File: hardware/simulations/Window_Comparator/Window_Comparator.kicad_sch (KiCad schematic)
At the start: 11 parts, among them U101 Opamp_Dual

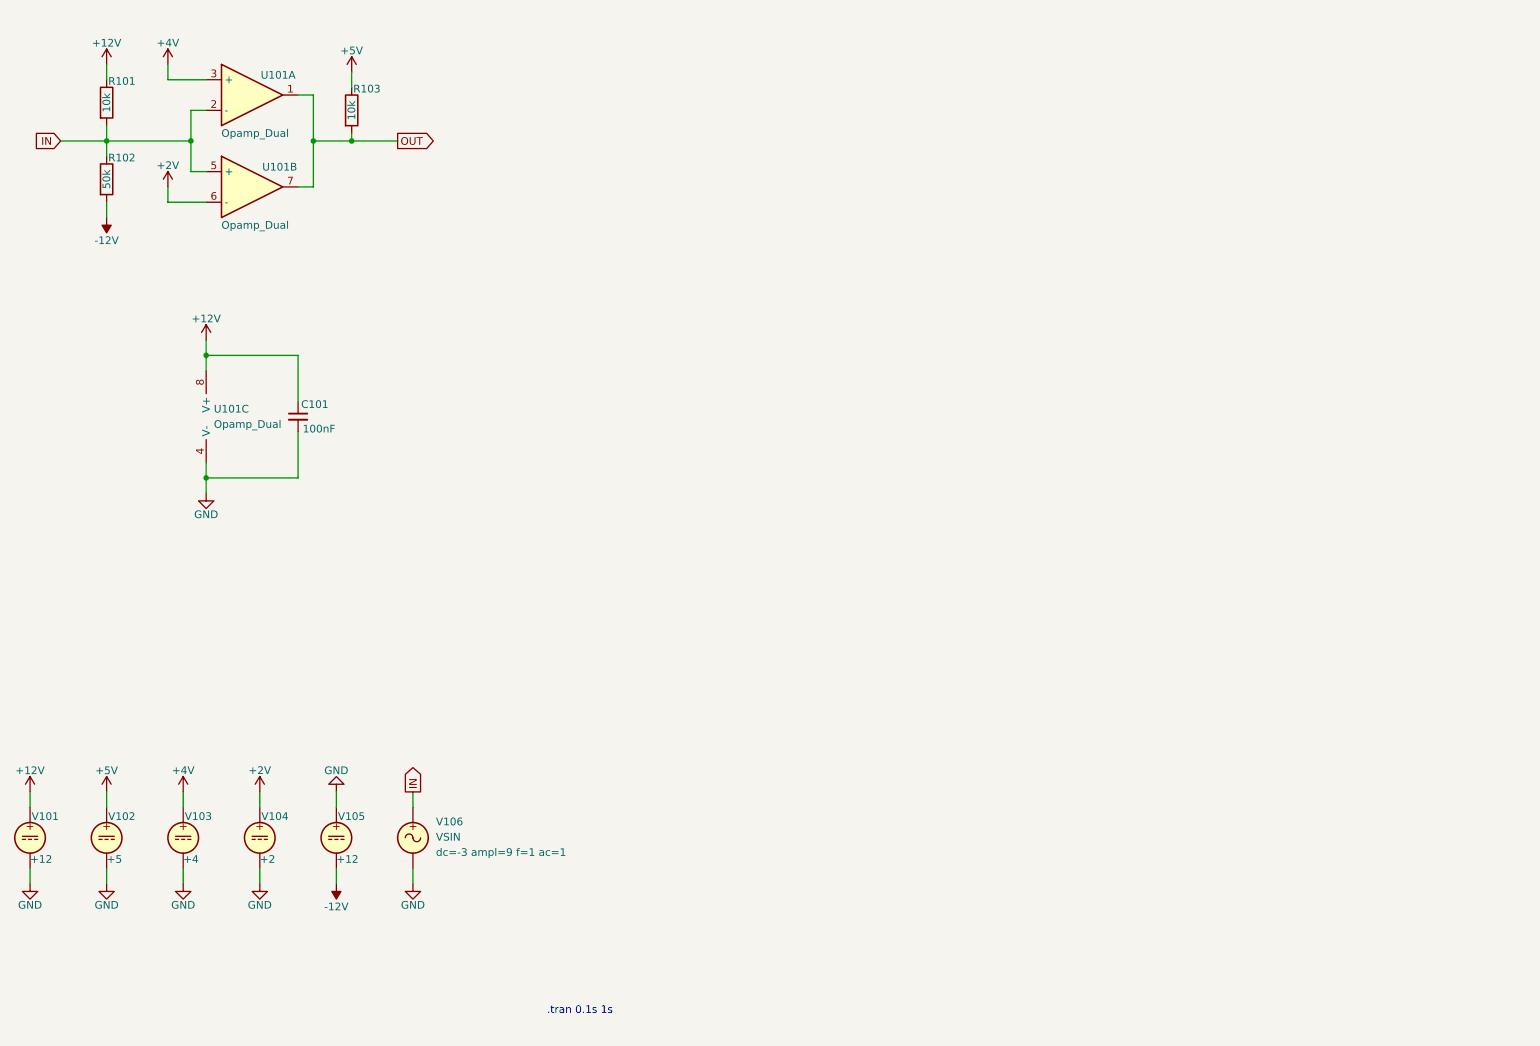
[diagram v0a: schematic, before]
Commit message: Quality assessment - Changes
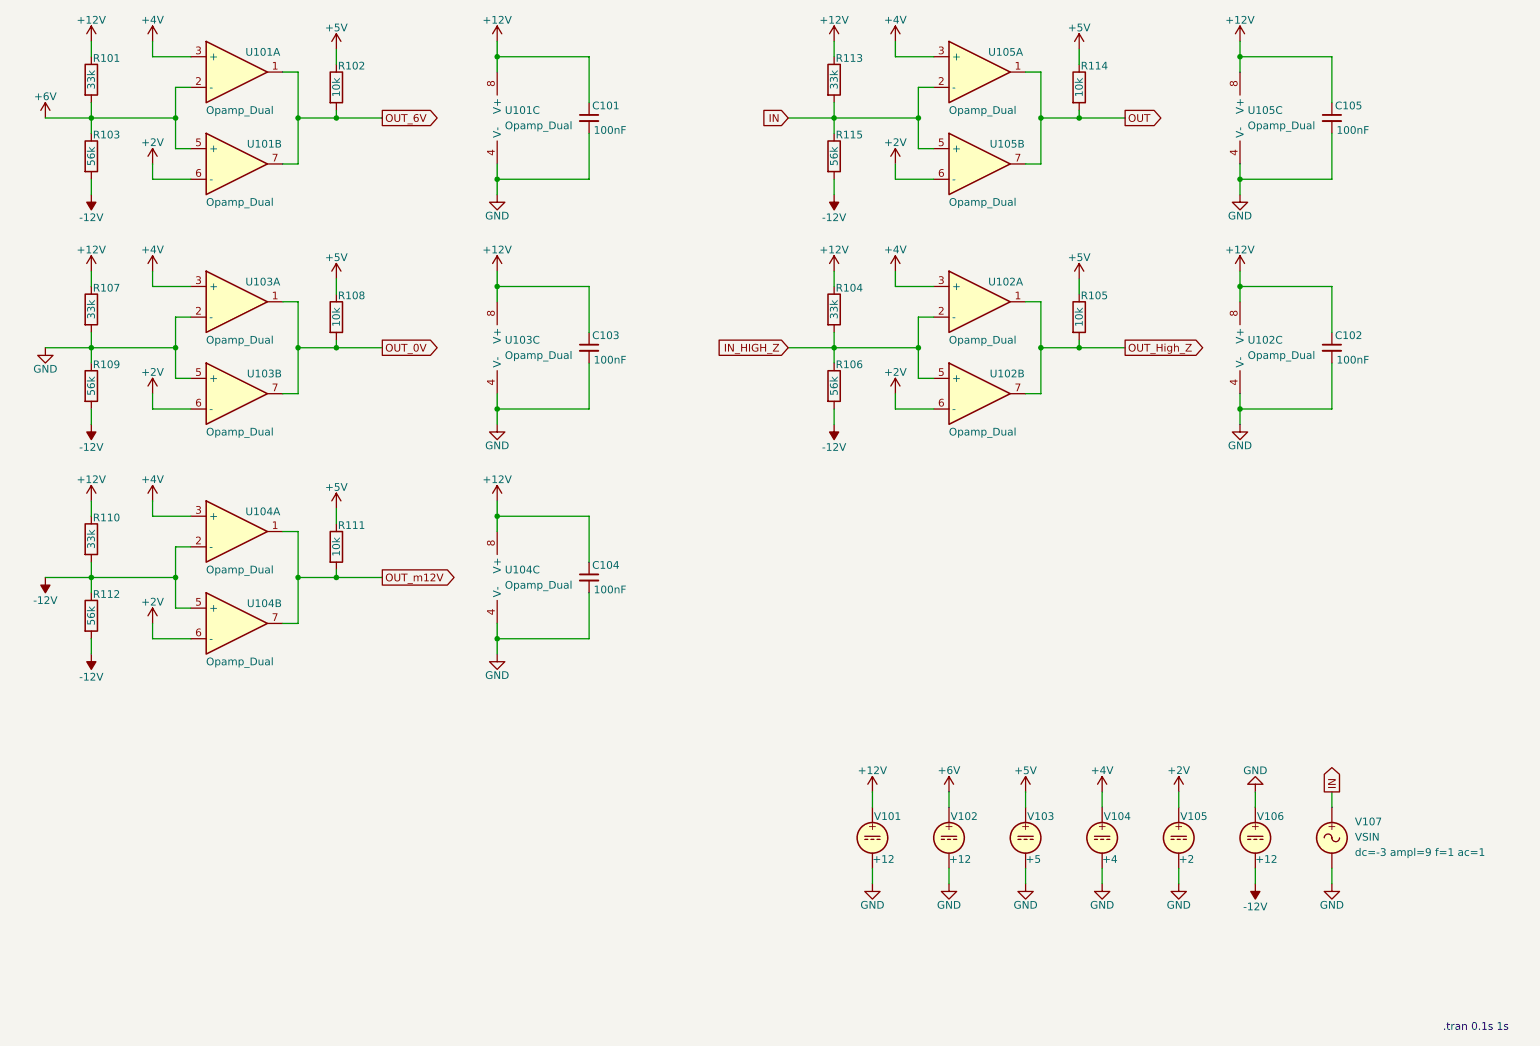
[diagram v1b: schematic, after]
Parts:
- added C102, C103, C104, C105: 100nF, Capacitor_THT:C_Disc_D5.0mm_W2.5mm_P5.00mm, symbol Device:C_Small
- added R104, R107, R110, R113: 33k, Resistor_THT:R_Axial_DIN0207_L6.3mm_D2.5mm_P7.62mm_Horizontal, symbol Device:R
- added R105, R108, R111, R114: 10k, Resistor_THT:R_Axial_DIN0207_L6.3mm_D2.5mm_P7.62mm_Horizontal, symbol Device:R
- added R106, R109, R112, R115: 56k, Resistor_THT:R_Axial_DIN0207_L6.3mm_D2.5mm_P7.62mm_Horizontal, symbol Device:R
- added U102, U103, U104, U105: Opamp_Dual, symbol Device:Opamp_Dual
- added V101: +12, symbol Simulation_SPICE:VDC
- R101: value 10k -> 33k
- R103: renamed from R102; value 50k -> 56k
- renumbered R103 to R102, V101 to V102, V102 to V103, V103 to V104, V104 to V105, V105 to V106, V106 to V107
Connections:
- net +12V: now also C102.1, C103.1, C104.1, C105.1, R104.1, R107.1, R110.1, R113.1, U102.8 (V+), U103.8 (V+), U104.8 (V+), U105.8 (V+), V101.1; no longer V102.1
- net +2V: now also U102.6 (-), U103.6 (-), U104.6 (-), U105.6 (-)
- net +4V: now also U102.3 (+), U103.3 (+), U104.3 (+), U105.3 (+)
- net +5V: now also R105.1, R108.1, R111.1, R114.1
- net -12V: now also R106.2, R109.2, R110.2, R112.1, R112.2, R115.2, U104.2 (-), U104.5 (+)
- net GND: now also C102.2, C103.2, C104.2, C105.2, R107.2, R109.1, U102.4 (V-), U103.2 (-), U103.4 (V-), U103.5 (+), U104.4 (V-), U105.4 (V-), V101.2
- net IN: now also R113.2, R115.1, U105.2 (-), U105.5 (+); no longer R101.2, R103.1, U101.2 (-), U101.5 (+)
- net OUT: now also R114.2, U105.1, U105.7; no longer R102.2, U101.1, U101.7
- new net +6V: R101.2, R103.1, U101.2 (-), U101.5 (+), V102.1
- new net IN_HIGH_Z: R104.2, R106.1, U102.2 (-), U102.5 (+)
- new net OUT_0V: R108.2, U103.1, U103.7
- new net OUT_6V: R102.2, U101.1, U101.7
- new net OUT_High_Z: R105.2, U102.1, U102.7
- new net OUT_m12V: R111.2, U104.1, U104.7
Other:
- moved on the sheet: C101, R101, R102, R103, U101A, U101B, U101C, V102, V103, V104, V105, V106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

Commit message: Added proof of concept Window comparator
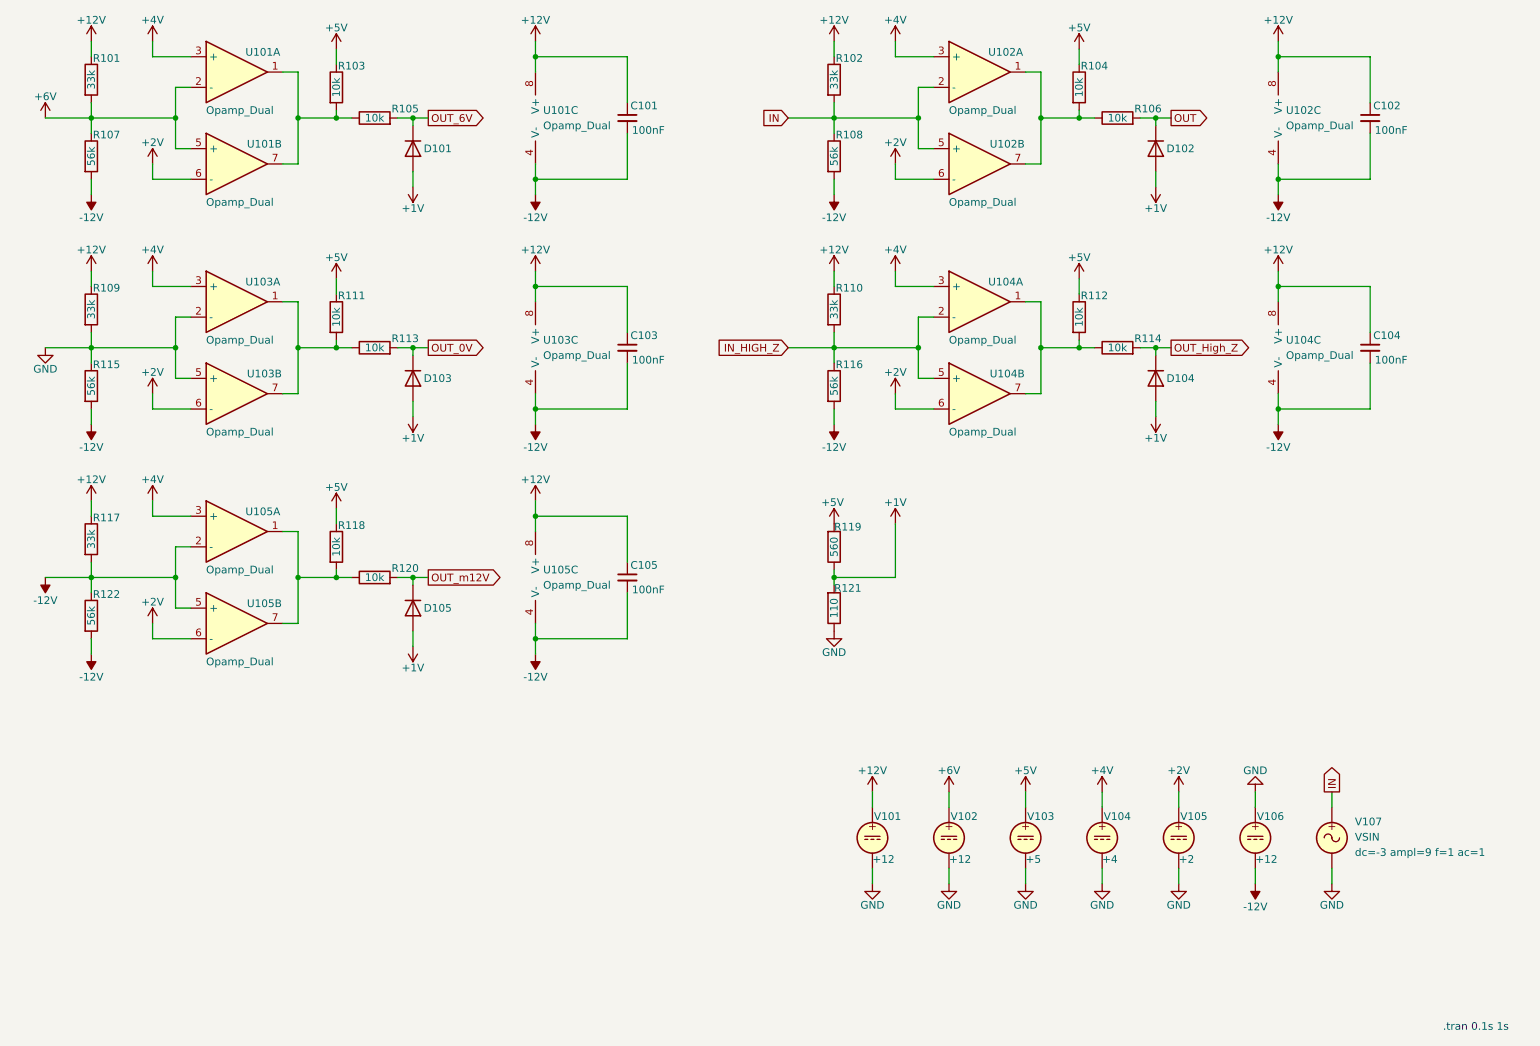
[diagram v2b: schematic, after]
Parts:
- added D101, D102, D103, D104, D105: D, symbol Device:D
- added R105, R106, R113, R114, R120: 10k, Resistor_THT:R_Axial_DIN0207_L6.3mm_D2.5mm_P7.62mm_Horizontal, symbol Device:R
- added R119: 560, Resistor_THT:R_Axial_DIN0207_L6.3mm_D2.5mm_P7.62mm_Horizontal, symbol Device:R
- added R121: 110, Resistor_THT:R_Axial_DIN0207_L6.3mm_D2.5mm_P7.62mm_Horizontal, symbol Device:R
- renumbered C105 to C102, C102 to C104, C104 to C105, R113 to R102, R102 to R103, R114 to R104, R103 to R107, R115 to R108, R107 to R109, R104 to R110, R108 to R111, R105 to R112, R109 to R115, R106 to R116, R110 to R117, R111 to R118, R112 to R122, U105 to U102, U102 to U104, U104 to U105
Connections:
- net +5V: now also R119.2
- net -12V: now also C101.2, C102.2, C103.2, C104.2, C105.2, U101.4 (V-), U102.4 (V-), U103.4 (V-), U104.4 (V-), U105.4 (V-)
- net GND: now also R121.1; no longer C101.2, C102.2, C103.2, C104.2, C105.2, U101.4 (V-), U102.4 (V-), U103.4 (V-), U104.4 (V-), U105.4 (V-)
- net OUT: now also D102.1 (K), R106.2; no longer R104.2, U102.1, U102.7
- net OUT_0V: now also D103.1 (K), R113.2; no longer R111.2, U103.1, U103.7
- net OUT_6V: now also D101.1 (K), R105.2; no longer R103.2, U101.1, U101.7
- net OUT_High_Z: now also D104.1 (K), R114.2; no longer R112.2, U104.1, U104.7
- net OUT_m12V: now also D105.1 (K), R120.2; no longer R118.2, U105.1, U105.7
- new net: R103.2, R105.1, U101.1, U101.7
- new net: R112.2, R114.1, U104.1, U104.7
- new net: R104.2, R106.1, U102.1, U102.7
- new net: R118.2, R120.1, U105.1, U105.7
- new net: R111.2, R113.1, U103.1, U103.7
- new net +1V: D101.2 (A), D102.2 (A), D103.2 (A), D104.2 (A), D105.2 (A), R119.1, R121.2
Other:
- moved on the sheet: C101, C102, C103, C104, C105, U101C, U102C, U103C, U104C, U105C
